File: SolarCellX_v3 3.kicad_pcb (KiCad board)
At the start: 6 copper layers, 48.4 x 48.4 mm, 55 parts, among them J1 XF2M-1015-1A, U2 Value, U3 TSL2561

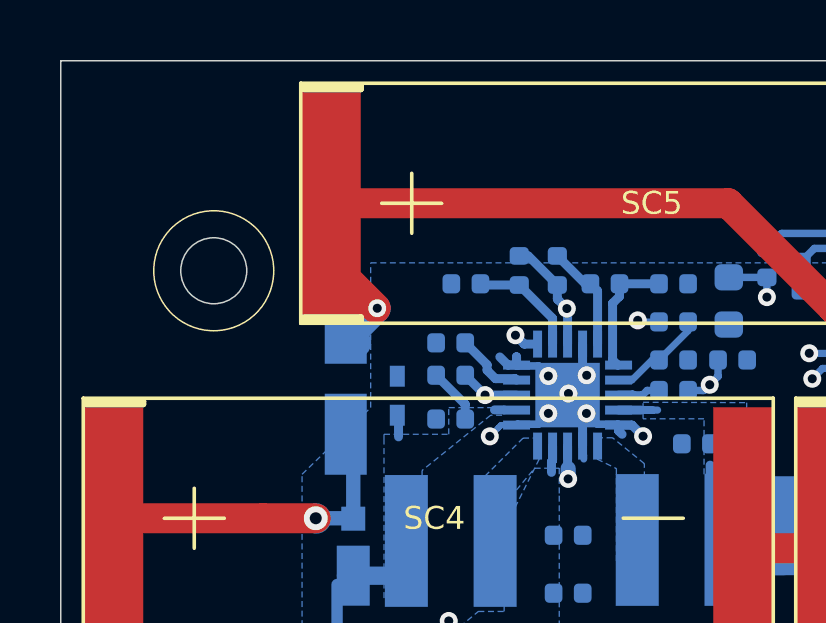
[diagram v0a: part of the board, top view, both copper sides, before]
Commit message: Changed magnetorquer coils
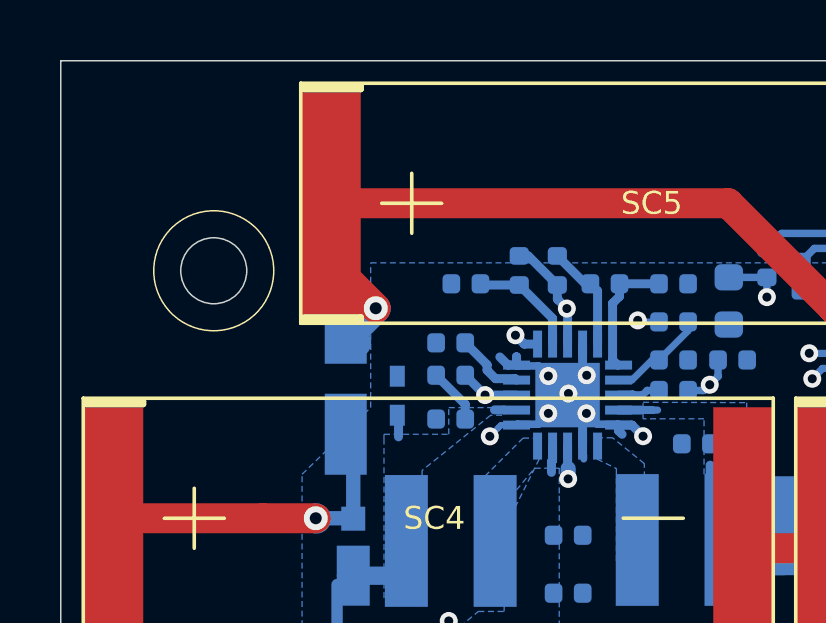
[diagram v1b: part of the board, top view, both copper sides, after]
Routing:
- net /coil: track 12877.3 -> 14544.2 mm
